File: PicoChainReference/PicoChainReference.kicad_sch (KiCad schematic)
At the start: 16 parts, among them J1 RJ45, J2 RJ45, J3 Conn 01x02, J4 Conn 01x02, J5 Conn 01x02, J6 Conn 01x02, U1 LM78M05_TO252, U2 PCA9615DP, U4 LM78M05_TO252, U5 LM1085-12

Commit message: Added licences and PDF schematics
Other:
- title: (none) -> PicoChain Generic Reference Device Implementation
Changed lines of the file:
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@@
 	(generator_version "8.0")
 	(paper "A4")
+	(title_block
+		(title "PicoChain Generic Reference Device Implementation")
+		(date "2024-08-22")
+		(rev "v1.1")
+		(comment 2 "http://www.tapr.org/OHL")
+		(comment 3 "Licence: The TAPR Open Hardware License")
+		(comment 4 "Author: Jason Alexander")
+	)
 	(junction
 		(at 106.68 58.42)

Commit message: Updated PicoChainZero base board.
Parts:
- added F1, F2: Fuse, Fuse:Fuse_0805_2012Metric, symbol Device:Fuse
- added U5: SRV05, Package_TO_SOT_SMD:SOT-23-6, symbol Power_Protection:SRV05-4
- J3: value Conn 01x02 -> +12V
- J4: value Conn 01x02 -> +5V(M)
- J5: value Conn 01x02 -> I2C
- J6: value Conn 01x02 -> +5V
- U1: value LM78M05_TO252 -> LM78M05
- U2: renamed from U4; value LM78M05_TO252 -> LM78M05
- U3: renamed from U5; value LM1085-12 -> LM1085
- renumbered U2 to U4
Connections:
- net +12V: now also F1.2; no longer J1.8
- net +24V: now also F2.2; no longer J1.2
- net +5V: now also U5.5 (VP)
- net GND: now also U5.2 (VN)
- net at J1.3, J2.3: now also U4.9 (DSDAM), U5.3 (IO2); no longer U4.6 (DSCLM)
- net at J1.4, J2.4: now also U4.6 (DSCLM), U5.4 (IO3); no longer U4.7 (DSCLP)
- net at J1.5, J2.5: now also U4.7 (DSCLP), U5.6 (IO4); no longer U4.8 (DSDAP)
- net at J1.6, J2.6: now also U4.8 (DSDAP), U5.1 (IO1); no longer U4.9 (DSDAM)
- new net: F1.1, J1.8
- new net: F2.1, J1.2
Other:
- moved on the sheet: J5, U4

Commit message: Updated to 1.2
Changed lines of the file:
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@@
 (kicad_sch
-	(version 20231120)
+	(version 20250114)
 	(generator "eeschema")
-	(generator_version "8.0")
+	(generator_version "9.0")
 	(paper "A4")
 	(title_block
 		(title "PicoChain Generic Reference Device Implementation")
 		(date "2024-08-22")
-		(rev "v1.1")
+		(rev "v1.2")
 		(comment 2 "http://www.tapr.org/OHL")
 		(comment 3 "Licence: The TAPR Open Hardware License")
@@
 		)
 	)
+	(embedded_fonts no)
 )

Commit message: Added more fuses to reference implementation
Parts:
- added F3, F4: Fuse, Fuse:Fuse_0805_2012Metric, symbol Device:Fuse
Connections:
- net +12V: now also F3.2; no longer J2.8
- net +24V: now also F4.2; no longer J2.2
- new net: F4.1, J2.2
- new net: F3.1, J2.8
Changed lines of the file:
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@@
 	(title_block
 		(title "PicoChain Generic Reference Device Implementation")
-		(date "2024-08-22")
+		(date "2025-04-21")
 		(rev "v1.2")
 		(comment 2 "http://www.tapr.org/OHL")
@@
 	(wire
 		(pts
+			(xy 99.06 97.79) (xy 100.33 97.79)
+		)
+		(stroke
+			(width 0)
+			(type default)
+		)
+	)
+	(wire
+		(pts
 			(xy 99.06 87.63) (xy 100.33 87.63)
 		)
@@
 	(wire
 		(pts
+			(xy 99.06 113.03) (xy 100.33 113.03)
+		)
+		(stroke
+			(width 0)
+			(type default)
+		)
+	)
+	(wire
+		(pts
 			(xy 99.06 74.93) (xy 100.33 74.93)
 		)
@@
 	(wire
 		(pts
-			(xy 99.06 97.79) (xy 100.33 97.79)
+			(xy 107.95 113.03) (xy 109.22 113.03)
 		)
 		(stroke
@@
 	(wire
 		(pts
-			(xy 99.06 113.03) (xy 100.33 113.03)
+			(xy 113.03 69.85) (xy 118.11 69.85)
 		)
 		(stroke
@@
 	(wire
 		(pts
-			(xy 113.03 69.85) (xy 118.11 69.85)
+			(xy 107.95 97.79) (xy 109.22 97.79)
 		)
 		(stroke
@@
 	)
 	(symbol
-		(lib_id "power:+24V")
-		(at 100.33 113.03 270)
-		(unit 1)
-		(exclude_from_sim no)
-		(in_bom yes)
-		(on_board yes)
-		(dnp no)
-		(property "Reference" "#PWR010"
-			(at 96.52 113.03 0)
-			(effects
-				(font
-					(size 1.27 1.27)
-				)
-				(hide yes)
-			)
-		)
-		(property "Value" "+24V"
-			(at 99.06 111.506 90)
-			(effects
-				(font
-					(size 1.27 1.27)
-				)
-				(justify left)
-			)
-		)
-		(property "Footprint" ""
-			(at 100.33 113.03 0)
-			(effects
-				(font
-					(size 1.27 1.27)
-				)
-				(hide yes)
-			)
-		)
-		(property "Datasheet" ""
-			(at 100.33 113.03 0)
-			(effects
-				(font
-					(size 1.27 1.27)
-				)
-				(hide yes)
-			)
-		)
-		(property "Description" "Power symbol creates a global label with name \"+24V\""
-			(at 100.33 113.03 0)
-			(effects
-				(font
-					(size 1.27 1.27)
-				)
-				(hide yes)
-			)
-		)
-		(pin "1"
-		)
-		(instances
-			(project "PicoChainReference"
-				(path "/bf05c66b-7ba7-46d1-8dac-29939cd00b00"
-					(reference "#PWR010")
-					(unit 1)
-				)
-			)
-		)
-	)
-	(symbol
 		(lib_id "Connector:Conn_01x02_Socket")
 		(at 71.12 88.9 0)
@@
 	(symbol
 		(lib_id "Device:Fuse")
+		(at 104.14 97.79 90)
+		(unit 1)
+		(exclude_from_sim no)
+		(in_bom yes)
+		(on_board yes)
+		(dnp no)
+		(property "Reference" "F3"
+			(at 104.14 96.266 90)
+			(effects
+				(font
+					(size 1.27 1.27)
+				)
+			)
+		)
+		(property "Value" "Fuse"
+			(at 104.14 99.568 90)
+			(effects
+				(font
+					(size 1.27 1.27)
+				)
+				(hide yes)
+			)
+		)
+		(property "Footprint" "Fuse:Fuse_0805_2012Metric"
+			(at 104.14 99.568 90)
+			(effects
+				(font
+					(size 1.27 1.27)
+				)
+				(hide yes)
+			)
+		)
+		(property "Datasheet" "~"
+			(at 104.14 97.79 0)
+			(effects
+				(font
+					(size 1.27 1.27)
+				)
+				(hide yes)
+			)
+		)
+		(property "Description" "Fuse"
+			(at 104.14 97.79 0)
+			(effects
+				(font
+					(size 1.27 1.27)
+				)
+				(hide yes)
+			)
+		)
+		(pin "2"
+		)
+		(pin "1"
+		)
+		(instances
+			(project "PicoChainReference"
+				(path "/bf05c66b-7ba7-46d1-8dac-29939cd00b00"
+					(reference "F3")
+					(unit 1)
+				)
+			)
+		)
+	)
+	(symbol
+		(lib_id "Device:Fuse")
 		(at 104.14 72.39 90)
 		(unit 1)
@@
 	)
 	(symbol
+		(lib_id "power:+24V")
+		(at 109.22 113.03 270)
+		(unit 1)
+		(exclude_from_sim no)
+		(in_bom yes)
+		(on_board yes)
+		(dnp no)
+		(property "Reference" "#PWR010"
+			(at 105.41 113.03 0)
+			(effects
+				(font
+					(size 1.27 1.27)
+				)
+				(hide yes)
+			)
+		)
+		(property "Value" "+24V"
+			(at 106.68 111.506 90)
+			(effects
+				(font
+					(size 1.27 1.27)
+				)
+				(justify left)
+			)
+		)
+		(property "Footprint" ""
+			(at 109.22 113.03 0)
+			(effects
+				(font
+					(size 1.27 1.27)
+				)
+				(hide yes)
+			)
+		)
+		(property "Datasheet" ""
+			(at 109.22 113.03 0)
+			(effects
+				(font
+					(size 1.27 1.27)
+				)
+				(hide yes)
+			)
+		)
+		(property "Description" "Power symbol creates a global label with name \"+24V\""
+			(at 109.22 113.03 0)
+			(effects
+				(font
+					(size 1.27 1.27)
+				)
+				(hide yes)
+			)
+		)
+		(pin "1"
+		)
+		(instances
+			(project "PicoChainReference"
+				(path "/bf05c66b-7ba7-46d1-8dac-29939cd00b00"
+					(reference "#PWR010")
+					(unit 1)
+				)
+			)
+		)
+	)
+	(symbol
 		(lib_id "power:GND")
 		(at 100.33 74.93 90)
@@
 	)
 	(symbol
+		(lib_id "Device:Fuse")
+		(at 104.14 113.03 90)
+		(unit 1)
+		(exclude_from_sim no)
+		(in_bom yes)
+		(on_board yes)
+		(dnp no)
+		(property "Reference" "F4"
+			(at 104.14 111.506 90)
+			(effects
+				(font
+					(size 1.27 1.27)
+				)
+			)
+		)
+		(property "Value" "Fuse"
+			(at 104.14 114.808 90)
+			(effects
+				(font
+					(size 1.27 1.27)
+				)
+				(hide yes)
+			)
+		)
+		(property "Footprint" "Fuse:Fuse_0805_2012Metric"
+			(at 104.14 114.808 90)
+			(effects
+				(font
+					(size 1.27 1.27)
+				)
+				(hide yes)
+			)
+		)
+		(property "Datasheet" "~"
+			(at 104.14 113.03 0)
+			(effects
+				(font
+					(size 1.27 1.27)
+				)
+				(hide yes)
+			)
+		)
+		(property "Description" "Fuse"
+			(at 104.14 113.03 0)
+			(effects
+				(font
+					(size 1.27 1.27)
+				)
+				(hide yes)
+			)
+		)
+		(pin "2"
+		)
+		(pin "1"
+		)
+		(instances
+			(project "PicoChainReference"
+				(path "/bf05c66b-7ba7-46d1-8dac-29939cd00b00"
+					(reference "F4")
+					(unit 1)
+				)
+			)
+		)
+	)
+	(symbol
 		(lib_id "power:+5V")
 		(at 76.2 48.26 270)
@@
 	(symbol
 		(lib_id "power:+12V")
-		(at 100.33 97.79 270)
+		(at 109.22 97.79 270)
 		(unit 1)
 		(exclude_from_sim no)
@@
 		(on_board yes)
 		(dnp no)
-		(property "Reference" "#PWR04"
-			(at 96.52 97.79 0)
+		(property "Reference" "#PWR024"
+			(at 105.41 97.79 0)
 			(effects
 				(font
@@
 		)
 		(property "Value" "+12V"
-			(at 99.06 96.266 90)
+			(at 106.68 96.266 90)
 			(effects
 				(font
@@
 		)
 		(property "Footprint" ""
-			(at 100.33 97.79 0)
+			(at 109.22 97.79 0)
 			(effects
 				(font
@@
 		)
 		(property "Datasheet" ""
-			(at 100.33 97.79 0)
+			(at 109.22 97.79 0)
 			(effects
 				(font
@@
 		)
 		(property "Description" "Power symbol creates a global label with name \"+12V\""
-			(at 100.33 97.79 0)
+			(at 109.22 97.79 0)
 			(effects
 				(font
@@
 			(project "PicoChainReference"
 				(path "/bf05c66b-7ba7-46d1-8dac-29939cd00b00"
-					(reference "#PWR04")
+					(reference "#PWR024")
 					(unit 1)
 				)

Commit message: Added decoupling capacitors to dI2C drivers (doh)
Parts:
- added C8: 10uF, Capacitor_Tantalum_SMD:CP_EIA-3216-18_Kemet-A, symbol Device:C_Polarized
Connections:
- net +5V: now also C8.1
- net GND: now also C8.2
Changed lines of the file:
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@@
 	)
 	(junction
+		(at 132.08 62.23)
+		(diameter 0)
+		(color 0 0 0 0)
+	)
+	(junction
 		(at 149.86 58.42)
 		(diameter 0)
@@
 	(wire
 		(pts
+			(xy 132.08 59.69) (xy 132.08 62.23)
+		)
+		(stroke
+			(width 0)
+			(type default)
+		)
+	)
+	(wire
+		(pts
 			(xy 99.06 107.95) (xy 115.57 107.95)
 		)
@@
 	(wire
 		(pts
+			(xy 132.08 62.23) (xy 132.08 64.77)
+		)
+		(stroke
+			(width 0)
+			(type default)
+		)
+	)
+	(wire
+		(pts
 			(xy 118.11 72.39) (xy 116.84 72.39)
 		)
@@
 	(wire
 		(pts
+			(xy 129.54 62.23) (xy 132.08 62.23)
+		)
+		(stroke
+			(width 0)
+			(type default)
+		)
+	)
+	(wire
+		(pts
 			(xy 99.06 115.57) (xy 100.33 115.57)
 		)
@@
 	(wire
 		(pts
+			(xy 119.38 62.23) (xy 121.92 62.23)
+		)
+		(stroke
+			(width 0)
+			(type default)
+		)
+	)
+	(wire
+		(pts
 			(xy 63.5 55.88) (xy 63.5 58.42)
 		)
@@
 	)
 	(symbol
+		(lib_id "power:GND")
+		(at 119.38 62.23 270)
+		(unit 1)
+		(exclude_from_sim no)
+		(in_bom yes)
+		(on_board yes)
+		(dnp no)
+		(property "Reference" "#PWR034"
+			(at 113.03 62.23 0)
+			(effects
+				(font
+					(size 1.27 1.27)
+				)
+				(hide yes)
+			)
+		)
+		(property "Value" "GND"
+			(at 116.078 62.23 0)
+			(effects
+				(font
+					(size 1.27 1.27)
+				)
+			)
+		)
+		(property "Footprint" ""
+			(at 119.38 62.23 0)
+			(effects
+				(font
+					(size 1.27 1.27)
+				)
+				(hide yes)
+			)
+		)
+		(property "Datasheet" ""
+			(at 119.38 62.23 0)
+			(effects
+				(font
+					(size 1.27 1.27)
+				)
+				(hide yes)
+			)
+		)
+		(property "Description" "Power symbol creates a global label with name \"GND\" , ground"
+			(at 119.38 62.23 0)
+			(effects
+				(font
+					(size 1.27 1.27)
+				)
+				(hide yes)
+			)
+		)
+		(pin "1"
+		)
+		(instances
+			(project "PicoChainReference"
+				(path "/bf05c66b-7ba7-46d1-8dac-29939cd00b00"
+					(reference "#PWR034")
+					(unit 1)
+				)
+			)
+		)
+	)
+	(symbol
 		(lib_id "Connector:Conn_01x02_Socket")
 		(at 71.12 88.9 0)
@@
 	)
 	(symbol
+		(lib_id "Device:C_Polarized")
+		(at 125.73 62.23 270)
+		(mirror x)
+		(unit 1)
+		(exclude_from_sim no)
+		(in_bom yes)
+		(on_board yes)
+		(dnp no)
+		(property "Reference" "C8"
+			(at 127.508 62.23 0)
+			(effects
+				(font
+					(size 1.27 1.27)
+				)
+				(justify left)
+			)
+		)
+		(property "Value" "10uF"
+			(at 123.698 64.77 0)
+			(effects
+				(font
+					(size 1.27 1.27)
+				)
+				(justify left)
+			)
+		)
+		(property "Footprint" "Capacitor_Tantalum_SMD:CP_EIA-3216-18_Kemet-A"
+			(at 121.92 61.2648 0)
+			(effects
+				(font
+					(size 1.27 1.27)
+				)
+				(hide yes)
+			)
+		)
+		(property "Datasheet" "~"
+			(at 125.73 62.23 0)
+			(effects
+				(font
+					(size 1.27 1.27)
+				)
+				(hide yes)
+			)
+		)
+		(property "Description" "Polarized capacitor"
+			(at 125.73 62.23 0)
+			(effects
+				(font
+					(size 1.27 1.27)
+				)
+				(hide yes)
+			)
+		)
+		(pin "1"
+		)
+		(pin "2"
+		)
+		(instances
+			(project "PicoChainReference"
+				(path "/bf05c66b-7ba7-46d1-8dac-29939cd00b00"
+					(reference "C8")
+					(unit 1)
+				)
+			)
+		)
+	)
+	(symbol
 		(lib_id "power:+24V")
 		(at 109.22 113.03 270)
@@
 	(symbol
 		(lib_id "power:+5V")
-		(at 132.08 64.77 0)
+		(at 132.08 59.69 0)
 		(unit 1)
 		(exclude_from_sim no)
@@
 		(dnp no)
 		(property "Reference" "#PWR014"
-			(at 132.08 68.58 0)
+			(at 132.08 63.5 0)
 			(effects
 				(font
@@
 		)
 		(property "Value" "+5V"
-			(at 130.048 60.96 0)
+			(at 130.048 55.88 0)
 			(effects
 				(font
@@
 		)
 		(property "Footprint" ""
-			(at 132.08 64.77 0)
+			(at 132.08 59.69 0)
 			(effects
 				(font
@@
 		)
 		(property "Datasheet" ""
-			(at 132.08 64.77 0)
+			(at 132.08 59.69 0)
 			(effects
 				(font
@@
 		)
 		(property "Description" "Power symbol creates a global label with name \"+5V\""
-			(at 132.08 64.77 0)
+			(at 132.08 59.69 0)
 			(effects
 				(font

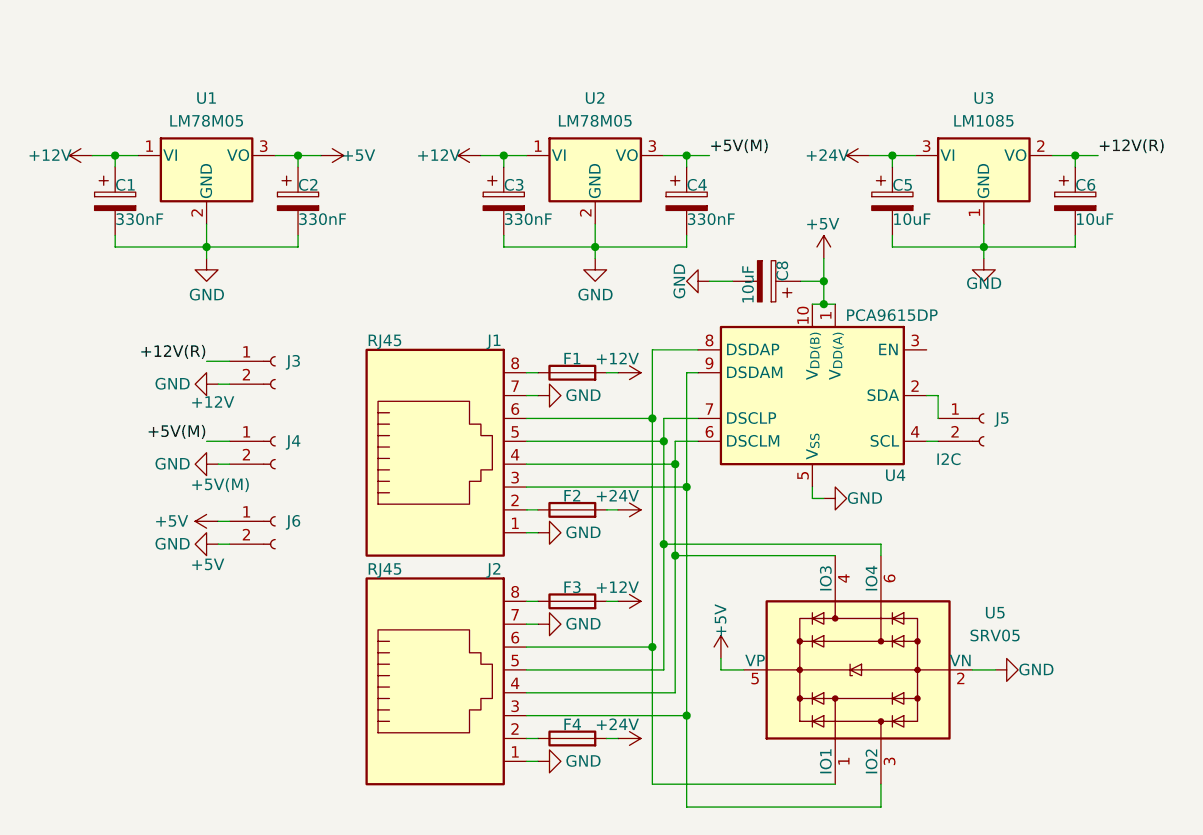
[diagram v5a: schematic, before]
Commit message: Adjusted schematics
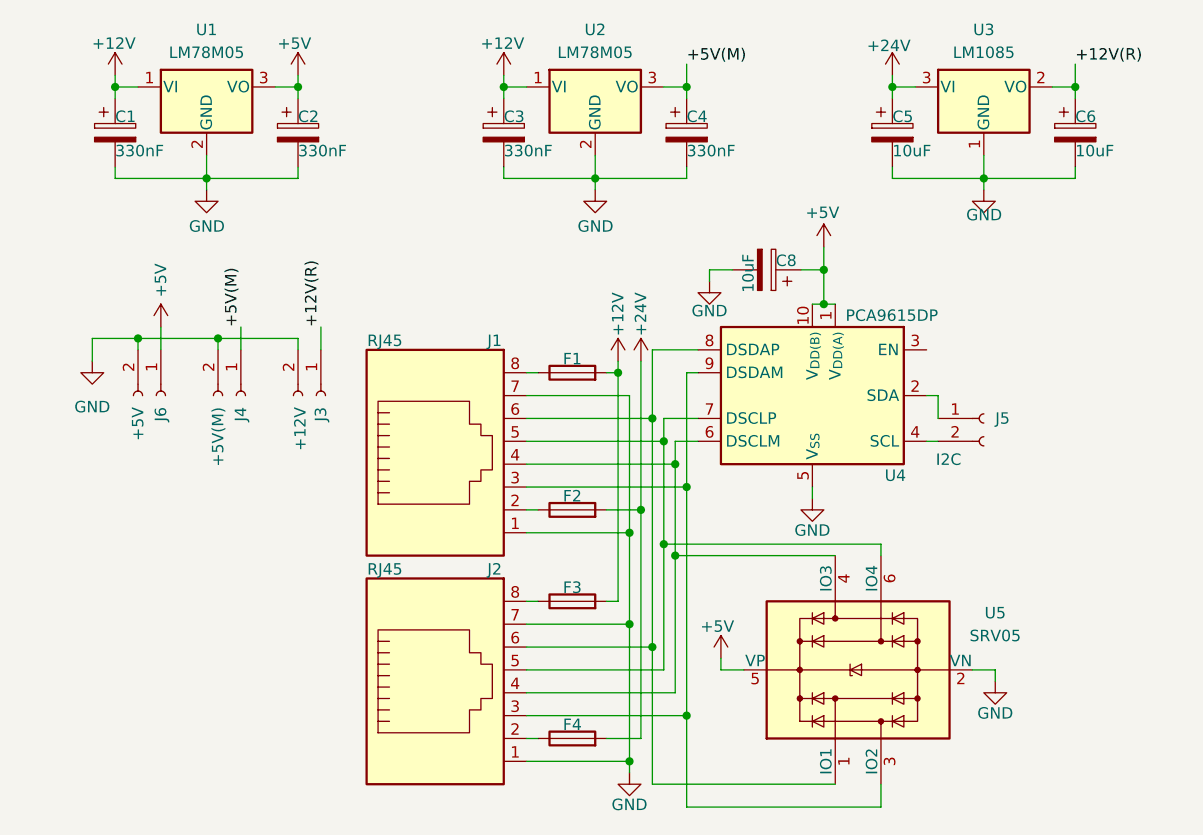
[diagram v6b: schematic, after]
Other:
- moved on the sheet: C1, C2, C3, C4, C5, C6, C8, J3, J4, J6, U1, U2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

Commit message: Finial changes before ordering first boards.
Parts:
- removed C8: 10uF, Capacitor_Tantalum_SMD:CP_EIA-3216-18_Kemet-A, symbol Device:C_Polarized
- added C13: 10uF, Capacitor_SMD:C_0805_2012Metric, symbol Device:C
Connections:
- net +5V: now also C13.2
- net GND: now also C13.1
